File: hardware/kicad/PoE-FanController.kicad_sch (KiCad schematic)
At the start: 31 parts, among them J2 FAN1, J3 FAN2, J4 FAN3, J5 FAN4, J6 Molex_KK254_3pin, J8 Waveshare_ESP32P4POEETH, U1 LM2587-12

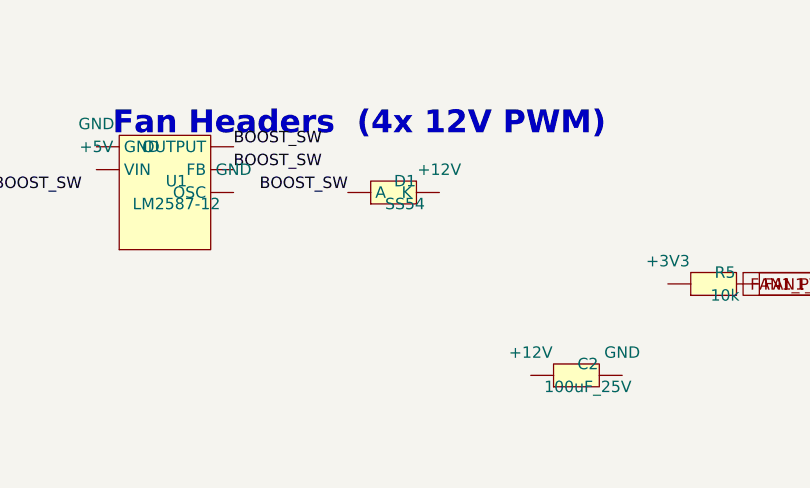
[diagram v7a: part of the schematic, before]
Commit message: fix(sch/pcb): replace D1 SS54 (SMA) with 1N5822 (DO-27)
SS54 SMA package is difficult to hand-solder. 1N5822 is electrically
equivalent but in a DO-27 axial through-hole package — much easier
to hand-solder.

Specs comparison:
  SS54:   40V / 5A / SMA (SMD)
  1N5822: 40V / 3A / DO-27 (THT) ← same voltage margin, sufficient current

Updated in:
  - components.py: symbol definition + D1 instantiation
  - kicad_sch: regenerated
  - kicad_pcb: D1 footprint swapped to Diode_THT:D_DO-27_P12.70mm_Horizontal
  - bom.csv: value updated to 1N5822

Co-authored-by: Copilot <223556219+Copilot@users.noreply.github.com>
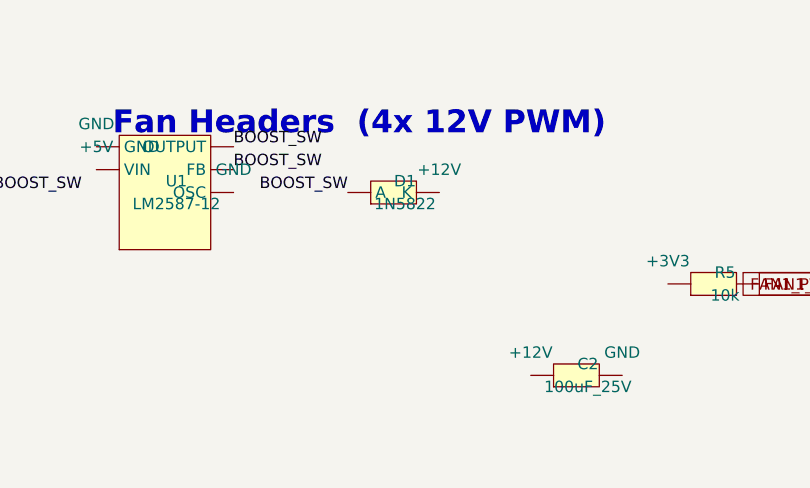
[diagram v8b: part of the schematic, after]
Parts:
- D1: value SS54 -> 1N5822; footprint Diode_SMD:D_SMA -> Diode_THT:D_DO-27_P12.70mm_Horizontal
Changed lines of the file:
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@@
       (at 245.1100 69.8500 0)
       (effects (font (size 1.27 1.27))))
-    (property "Value" "SS54"
+    (property "Value" "1N5822"
       (at 245.1100 72.3900 0)
       (effects (font (size 1.27 1.27))))
-    (property "Footprint" "Diode_SMD:D_SMA"
+    (property "Footprint" "Diode_THT:D_DO-27_P12.70mm_Horizontal"
       (at 243.8400 71.1200 0)
       (hide yes)
